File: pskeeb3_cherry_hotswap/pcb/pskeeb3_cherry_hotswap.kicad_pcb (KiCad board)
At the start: 2 copper layers, 131.7 x 109.6 mm, 42 parts, among them J1 OLED, K11 KEYSW, K12 KEYSW, K13 KEYSW, K14 KEYSW, K15 KEYSW, K21 KEYSW, K22 KEYSW, K23 KEYSW, K24 KEYSW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

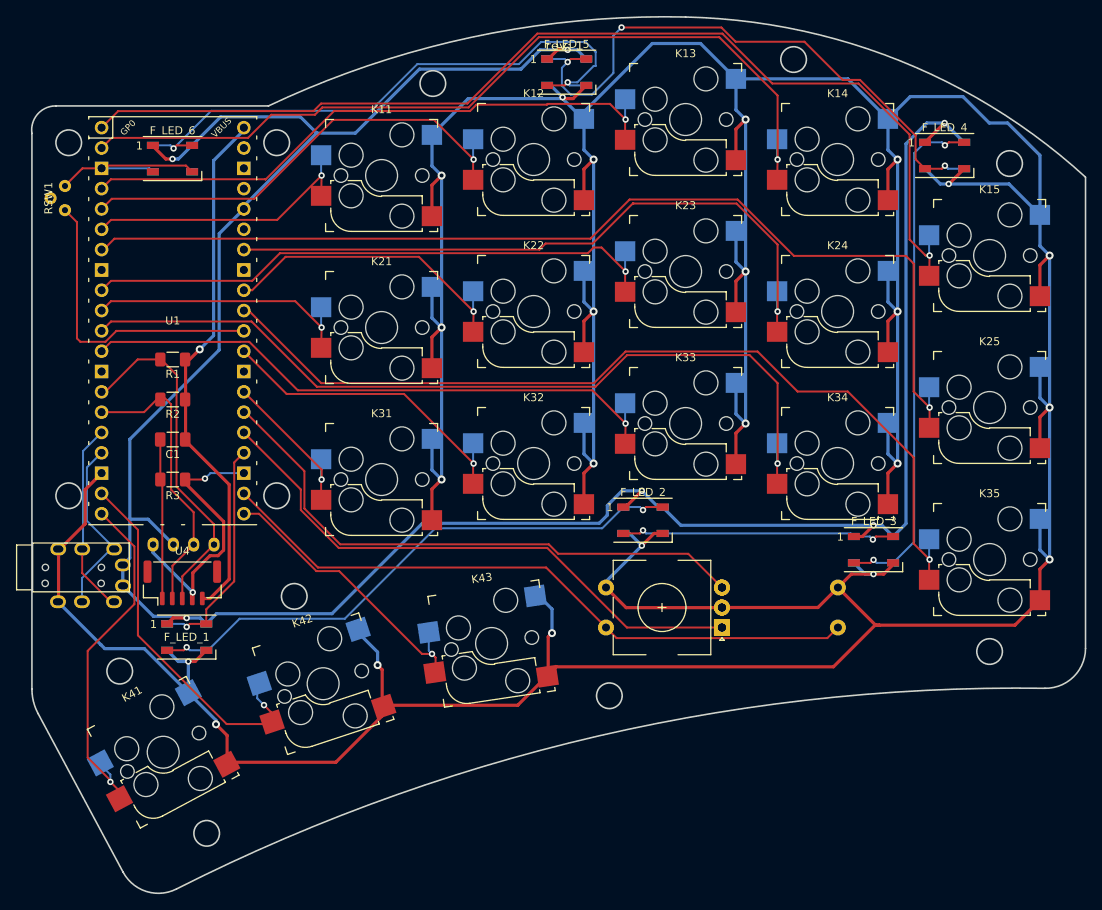
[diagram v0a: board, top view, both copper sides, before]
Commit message: refactor: increase footprint pads for easier soldering
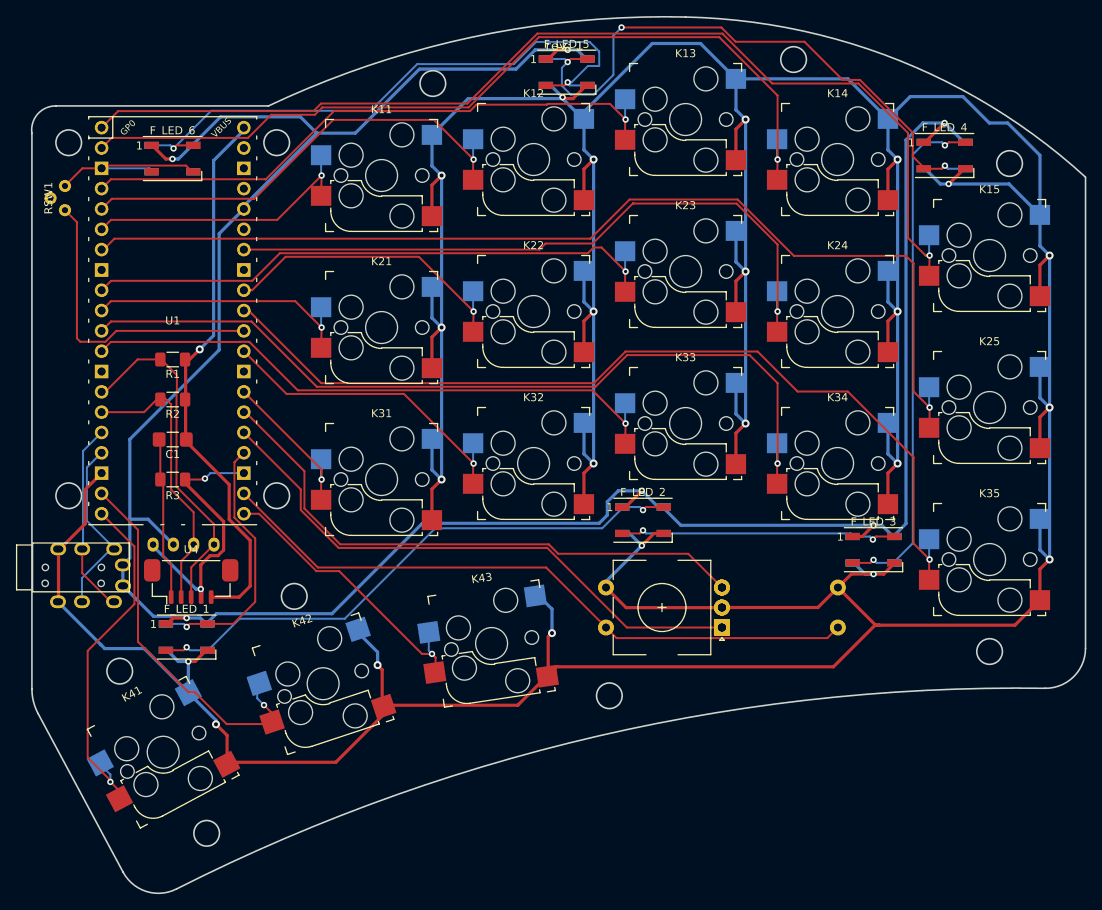
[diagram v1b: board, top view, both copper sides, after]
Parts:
- B_LED_1, B_LED_2, B_LED_3, B_LED_4, B_LED_5, B_LED_6, F_LED_1, F_LED_2, F_LED_3, F_LED_4, F_LED_5, F_LED_6: footprint LED_SMD:LED_WS2812B_PLCC4_5.0x5.0mm_P3.2mm -> kwkb-footprint:LED_WS2812B_PLCC4_5.0x5.0mm_P3.2mm
- C1: footprint Capacitor_SMD:C_1206_3216Metric_Pad1.33x1.80mm_HandSolder -> kwkb-footprint:C_1206_3216Metric_Pad1.33x1.80mm_HandSolder
- U4: footprint Connector_JST:JST_GH_BM05B-GHS-TBT_1x05-1MP_P1.25mm_Vertical -> kwkb-footprint:JST_GH_BM05B-GHS-TBT_1x05-1MP_P1.25mm_Vertical
- moved U4 1.12 mm to (72.7, 100.8)
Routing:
- net LED: track 28.5 -> 32.7 mm
- net +5V: track 65.7 -> 68.8 mm
- net Net-(B_LED_5-DOUT): track 75.4 -> 76.3 mm
- net TP_CLK/I2C1_SCL: track 36.6 -> 36.0 mm
- net TP_DAT/I2C1_SDA: track 43.0 -> 42.3 mm
- net +3V3: track 318.3 -> 318.9 mm
